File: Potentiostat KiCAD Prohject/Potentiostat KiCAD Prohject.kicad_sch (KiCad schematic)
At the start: 30 parts, among them K1 DIPxx-1Axx-12xD, U1 OPA2277, U2 TL074, U3 RP2040, U4 OPA2277, U5 INA128, U7 INA128, U8 REF3033, U9 INA128

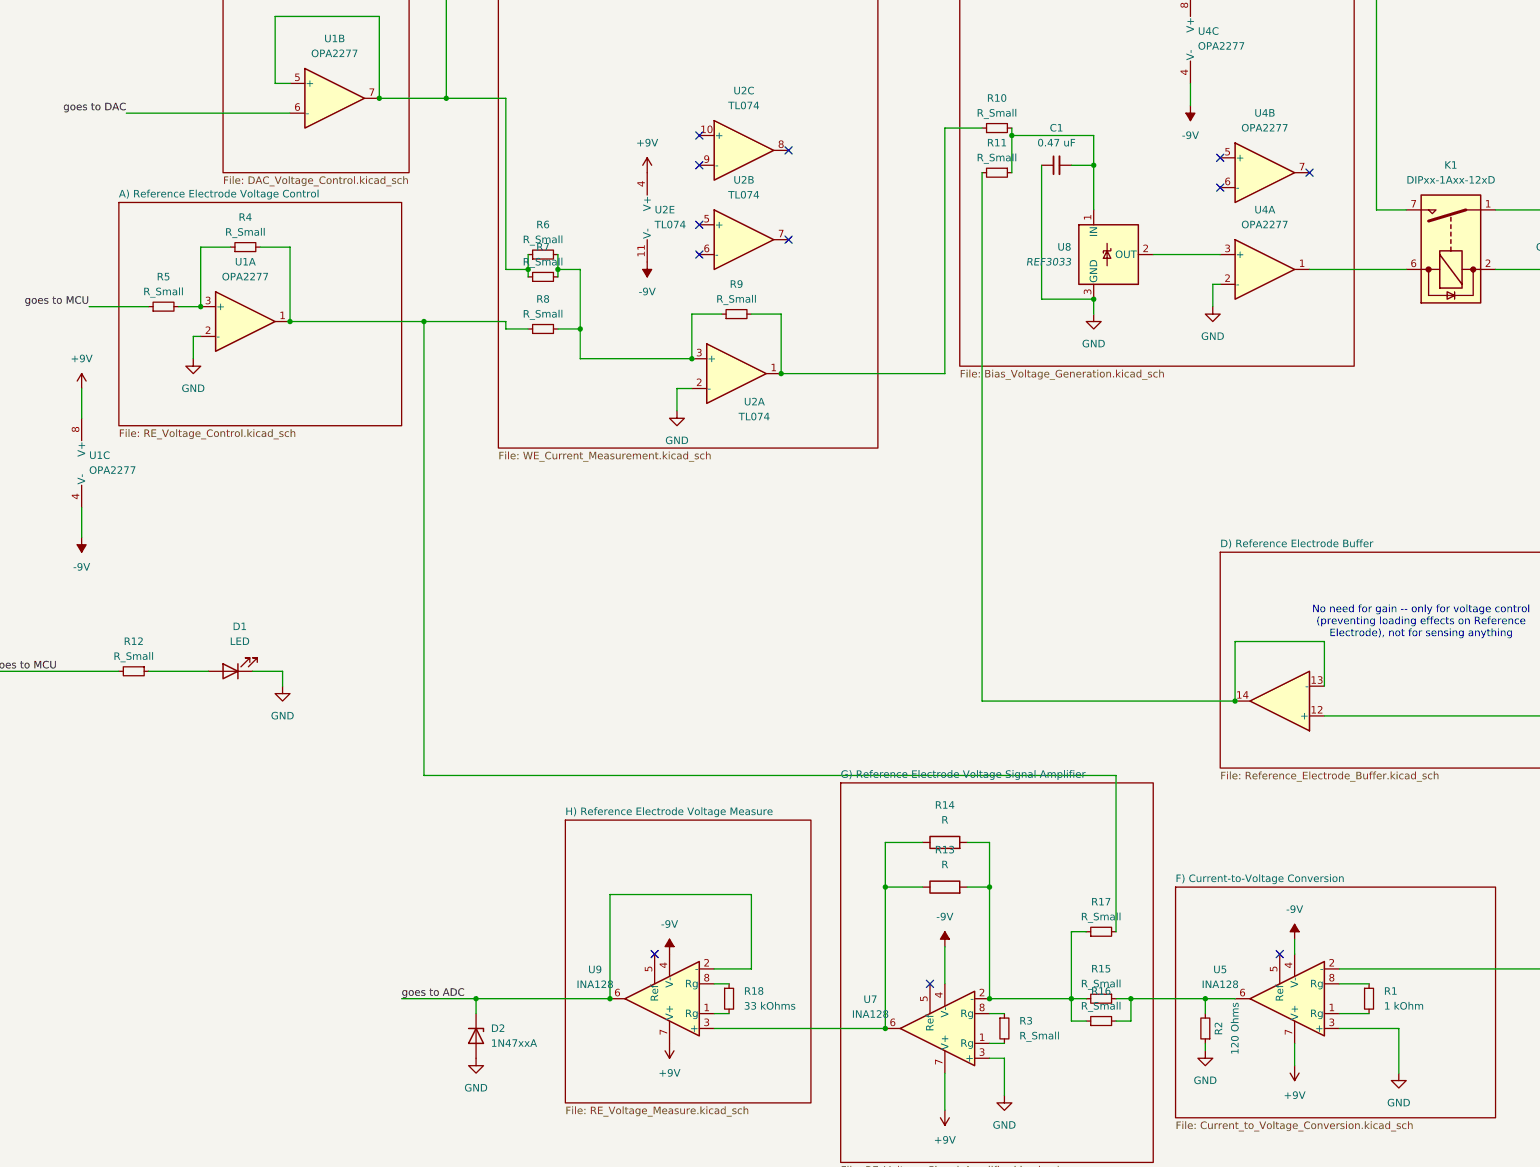
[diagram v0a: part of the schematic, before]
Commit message: changed resistor values
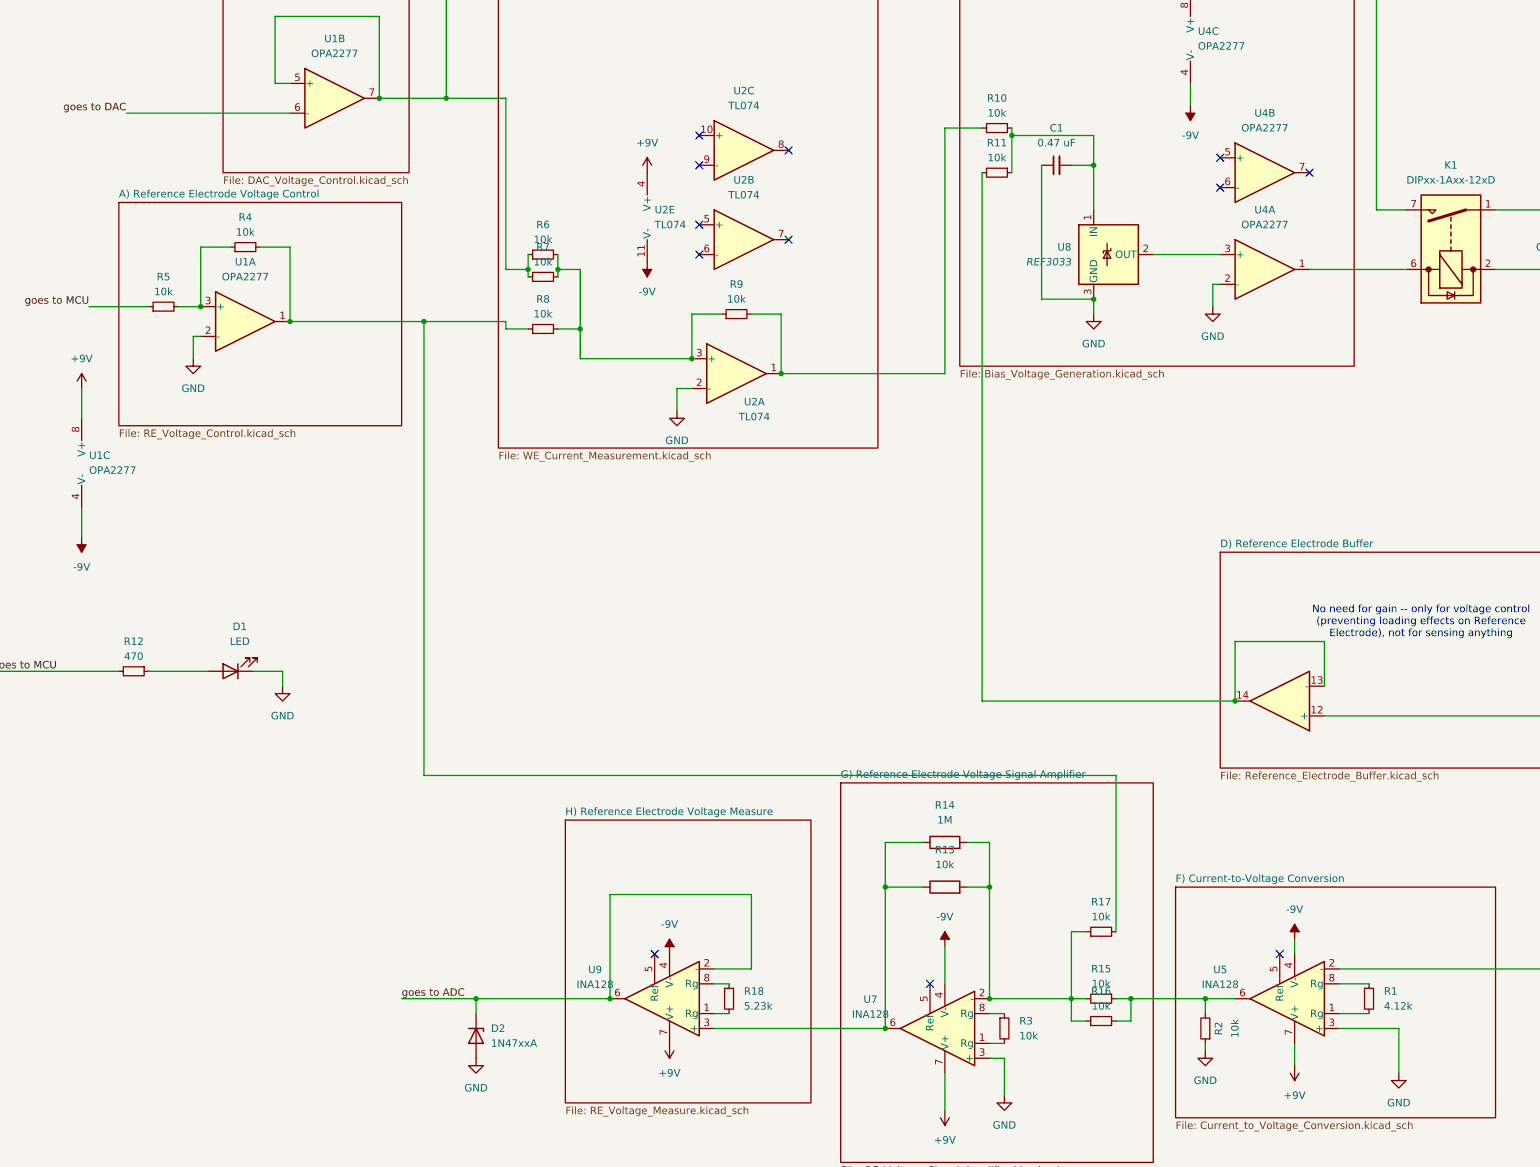
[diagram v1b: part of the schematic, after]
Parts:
- R1: value 1 kOhm -> 4.12k
- R10, R11, R15, R16, R17, R3, R4, R5, R6, R7, R8, R9: value R_Small -> 10k
- R12: value R_Small -> 470
- R13: value R -> 10k
- R14: value R -> 1M
- R18: value 33 kOhms -> 5.23k
- R2: value 120 Ohms -> 10k
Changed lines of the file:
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@@
 	(label "Working Electrode"
 		(at 495.3 283.21 0)
+		(fields_autoplaced yes)
 		(effects
 			(font
@@
 	(label "Working Electrode"
 		(at 495.3 163.83 0)
+		(fields_autoplaced yes)
 		(effects
 			(font
@@
 	(label "goes to MCU"
 		(at 457.2 116.84 0)
+		(fields_autoplaced yes)
 		(effects
 			(font
@@
 	(label "goes to ADC"
 		(at 290.83 288.29 0)
+		(fields_autoplaced yes)
 		(effects
 			(font
@@
 	(label "goes to ADC"
 		(at 247.65 102.87 180)
+		(fields_autoplaced yes)
 		(effects
 			(font
@@
 	(label "goes to MCU"
 		(at 237.49 170.18 180)
+		(fields_autoplaced yes)
 		(effects
 			(font
@@
 	(label "goes to DAC"
 		(at 243.84 137.16 180)
+		(fields_autoplaced yes)
 		(effects
 			(font
@@
 	(label "Reference Electrode"
 		(at 492.76 240.03 0)
+		(fields_autoplaced yes)
 		(effects
 			(font
@@
 	(label "goes to MCU"
 		(at 220.98 232.41 0)
+		(fields_autoplaced yes)
 		(effects
 			(font
@@
 			)
 		)
-		(property "Value" "1 kOhm"
+		(property "Value" "4.12k"
 			(at 458.47 289.5599 0)
 			(effects
@@
 			)
 		)
-		(property "Value" "R_Small"
+		(property "Value" "470"
 			(at 245.11 229.87 90)
 			(effects
@@
 			)
 		)
-		(property "Value" "R_Small"
+		(property "Value" "10k"
 			(at 410.21 274.32 90)
 			(effects
@@
 			)
 		)
-		(property "Value" "R_Small"
+		(property "Value" "10k"
 			(at 396.24 294.6399 0)
 			(effects
@@
 			)
 		)
-		(property "Value" "R_Small"
+		(property "Value" "10k"
 			(at 264.16 157.48 90)
 			(effects
@@
 			)
 		)
-		(property "Value" "R"
+		(property "Value" "10k"
 			(at 383.54 265.43 90)
 			(effects
@@
 			)
 		)
-		(property "Value" "R_Small"
+		(property "Value" "10k"
 			(at 314.96 171.45 90)
 			(effects
@@
 			)
 		)
-		(property "Value" "R_Small"
+		(property "Value" "10k"
 			(at 392.43 144.78 90)
 			(effects
@@
 			)
 		)
-		(property "Value" "R_Small"
+		(property "Value" "10k"
 			(at 314.96 162.56 90)
 			(effects
@@
 			)
 		)
-		(property "Value" "R"
+		(property "Value" "1M"
 			(at 383.54 257.81 90)
 			(effects
@@
 			)
 		)
-		(property "Value" "120 Ohms"
+		(property "Value" "10k"
 			(at 433.07 293.37 90)
 			(effects
@@
 			)
 		)
-		(property "Value" "33 kOhms"
+		(property "Value" "5.23k"
 			(at 349.25 289.5599 0)
 			(effects
@@
 			)
 		)
-		(property "Value" "R_Small"
+		(property "Value" "10k"
 			(at 347.98 168.91 90)
 			(effects
@@
 			)
 		)
-		(property "Value" "R_Small"
+		(property "Value" "10k"
 			(at 410.21 289.56 90)
 			(effects
@@
 			)
 		)
-		(property "Value" "R_Small"
+		(property "Value" "10k"
 			(at 392.43 137.16 90)
 			(effects
@@
 			)
 		)
-		(property "Value" "R_Small"
+		(property "Value" "10k"
 			(at 314.96 158.75 90)
 			(effects
@@
 			)
 		)
-		(property "Value" "R_Small"
+		(property "Value" "10k"
 			(at 250.19 167.64 90)
 			(effects
@@
 			)
 		)
-		(property "Value" "R_Small"
+		(property "Value" "10k"
 			(at 410.21 285.75 90)
 			(effects
